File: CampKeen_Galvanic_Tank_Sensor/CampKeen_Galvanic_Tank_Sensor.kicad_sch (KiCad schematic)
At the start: 24 parts, among them J1 Power_And_CAN, J2 TankInputs, J6 Screw_Terminal_01x02, Q1 IRF9Z34NPBF, Q30 2N7000, Q32 IRF9Z34NPBF, U1 3568, U5 3568

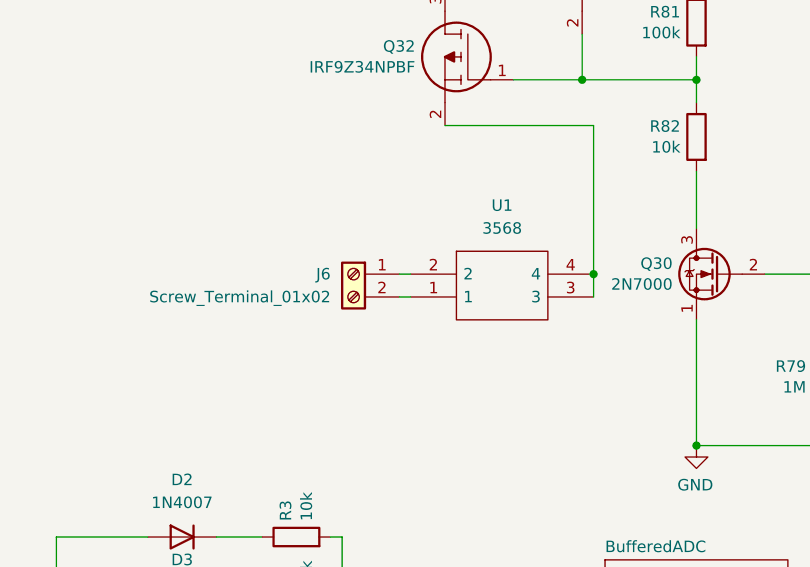
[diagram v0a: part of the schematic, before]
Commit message: hardware looks to be done. routed and DRC'ed needs to be sent off to be fabbed.
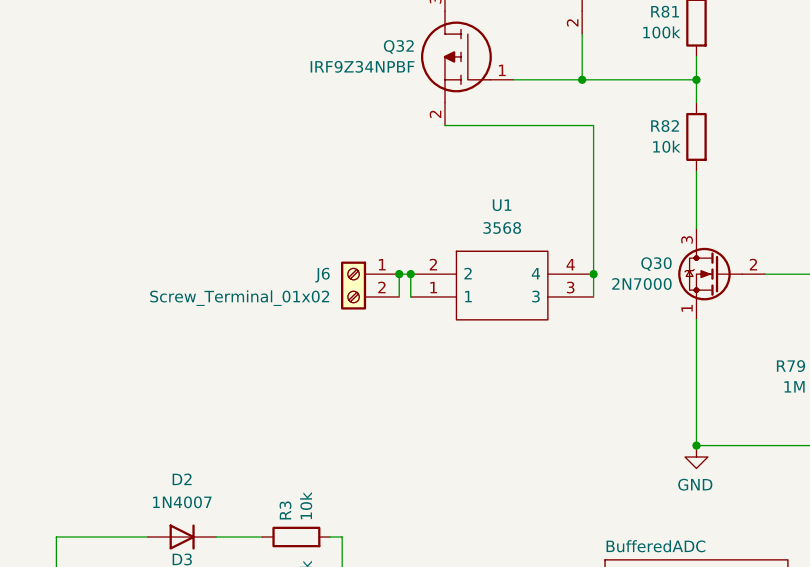
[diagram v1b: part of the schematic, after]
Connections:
- net at J6.2 (Pin_2), U1.1: now also J6.1 (Pin_1), U1.2
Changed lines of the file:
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@@
+	)
+	(junction
+		(at 72.39 118.11)
+		(diameter 0)
+		(color 0 0 0 0)
 	)
 	(junction
@@
 	)
 	(junction
+		(at 73.66 118.11)
+		(diameter 0)
+		(color 0 0 0 0)
+	)
+	(junction
 		(at 92.71 96.52)
 		(diameter 0)
@@
 	(wire
 		(pts
+			(xy 73.66 118.11) (xy 73.66 120.65)
+		)
+		(stroke
+			(width 0)
+			(type default)
+		)
+	)
+	(wire
+		(pts
 			(xy 231.14 129.54) (xy 231.14 133.35)
 		)
@@
 	(wire
 		(pts
-			(xy 72.39 120.65) (xy 73.66 120.65)
-		)
-		(stroke
-			(width 0)
-			(type default)
-		)
-	)
-	(wire
-		(pts
 			(xy 163.83 59.69) (xy 171.45 59.69)
 		)
@@
 		)
 		(stroke
+			(width 0)
+			(type default)
+		)
+	)
+	(wire
+		(pts
+			(xy 72.39 118.11) (xy 72.39 120.65)
+		)
+		(stroke
